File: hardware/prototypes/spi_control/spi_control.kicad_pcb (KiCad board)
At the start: 4 copper layers, 66.9 x 43.2 mm, 86 parts, among them J1 USB_B_Micro, J39 Versa_1, J40 Versa_2, U1 ST1L08SPU33R, U2 MCP2210-I_MQ, U3 ADAR7251, U4 BGT24_Module, Y1 12MHZ, Y2 40MHz

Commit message: Nov 17 Issues 1-22 complete.
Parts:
- removed G***: LOGO, bloop:meseek
- removed the REF** at (77.5, 84.4)
- removed the REF** at (77.5, 68.6)
- removed the REF** at (120.0, 93.0)
- removed the REF** at (120.0, 60.0)
- removed the REF** at (61.0, 93.1)
- removed the REF** at (61.0, 60.0)
- added H1: MountingHole_2.2mm_M2_Pad_Via, MountingHole:MountingHole_2.2mm_M2_Pad_Via, F.Cu at (116.9, 90.5)
- added H2: MountingHole_2.2mm_M2_Pad_Via, MountingHole:MountingHole_2.2mm_M2_Pad_Via, F.Cu at (116.9, 123.6)
- added H3: MountingHole_2.2mm_M2_Pad_Via, MountingHole:MountingHole_2.2mm_M2_Pad_Via, F.Cu at (175.9, 123.5)
- added H4: MountingHole_2.2mm_M2_Pad_Via, MountingHole:MountingHole_2.2mm_M2_Pad_Via, F.Cu at (175.9, 90.5)
- added H5: MountingHole_2.2mm_M2_Pad_Via, MountingHole:MountingHole_2.2mm_M2_Pad_Via, F.Cu at (133.3, 99.1)
- added H6: MountingHole_2.2mm_M2_Pad_Via, MountingHole:MountingHole_2.2mm_M2_Pad_Via, F.Cu at (133.3, 114.9)
- added REF**: OSHW-Logo2_7.3x6mm_SilkScreen, Symbol:OSHW-Logo2_7.3x6mm_SilkScreen, F.Cu at (166.4, 123.2)
- moved C1 63.7 mm to (171.0, 108.3)
- moved C11 63.7 mm to (134.0, 106.2)
- moved C14 63.7 mm to (132.3, 108.0)
- moved C15 63.7 mm to (132.3, 105.7)
- moved C16 63.7 mm to (132.3, 103.3)
- moved C18 63.7 mm to (166.0, 105.0)
- moved C22 63.7 mm to (128.0, 102.9)
- moved C30 63.7 mm to (125.3, 101.9)
- moved C38 63.7 mm to (126.3, 113.3)
- moved C42 63.7 mm to (125.6, 112.5)
- moved C5 63.7 mm to (134.0, 109.9)
- moved C6 63.7 mm to (134.0, 107.3)
- moved C9 63.7 mm to (134.0, 111.1)
- moved D1 63.7 mm to (171.6, 105.9)
- moved D3 63.7 mm to (178.6, 97.2)
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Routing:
- net GND: vias 54 -> 261
- net GNDA: vias 22 -> 52
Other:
- net class Default: clearance 0.2 -> 0.127; via_dia 0.4 -> 0.45
- net class Power: clearance 0.2 -> 0.127; via_dia 0.4 -> 0.45
- rule trace_clearance: 0.2 -> 0.127
- rule via_min_size: 0.4 -> 0.45
- board text added: "P_3V3"
- board text added: "P_5V"
- board text added: "Rev A."
- board text added: "SPI"
- board text removed: "Top - SIGNAL Inner Layer 1 - GND Inner Layer 2 - Power Bottom - SIGNAL"

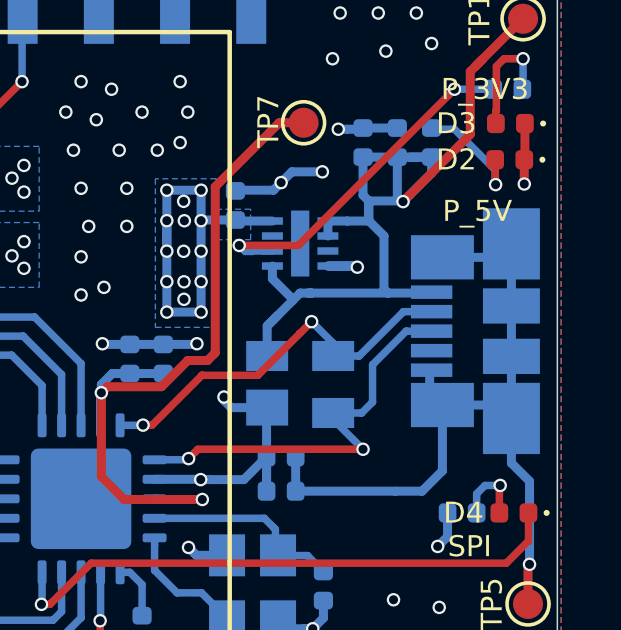
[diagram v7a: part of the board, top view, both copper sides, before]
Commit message: Added Keystone GND probe point.
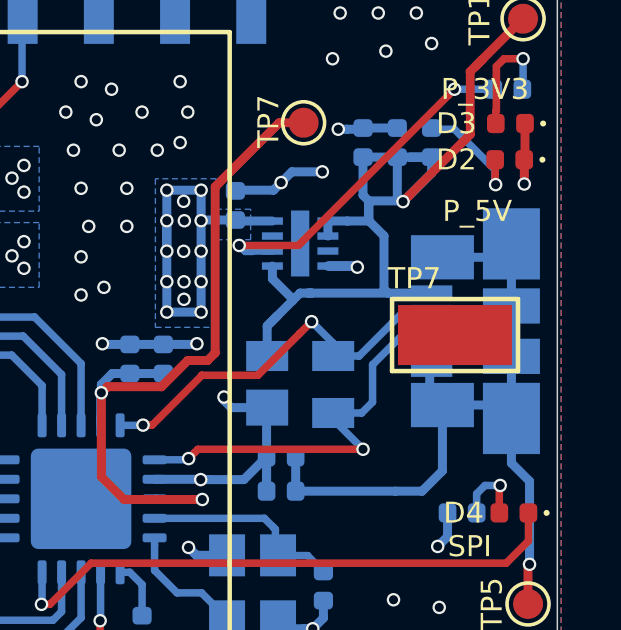
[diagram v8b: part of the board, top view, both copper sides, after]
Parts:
- added TP7: TestPoint_Keystone_5019_Minature, TestPoint:TestPoint_Keystone_5019_Minature, F.Cu at (176.8, 104.2)
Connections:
- H1 pad 1: (no net) -> GND
- H2 pad 1: (no net) -> GND
- H3 pad 1: (no net) -> GND
- H4 pad 1: (no net) -> GND
- H5 pad 1: (no net) -> GND
- H6 pad 1: (no net) -> GND
